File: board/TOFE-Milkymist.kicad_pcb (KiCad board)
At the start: 2 copper layers, 1 part

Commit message: Creating TOFE-Milkymist!
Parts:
- removed the U? at (148.4, 164.6)
- added U?: TOFE_Milkymist_Expansion_Board_8x_FullHeight, TOFE_8X_FullHeight, F.Cu at (125.1, 196.7)

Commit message: Initial version from on 2015-11-03
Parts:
- removed U?: TOFE_Milkymist_Expansion_Board_8x_FullHeight, TOFE_8X_FullHeight
- added 1PIN: P***, MH-4MM, F.Cu at (180.8, 64.5)
- added 1PIN: P***, MH-4MM, F.Cu at (181.1, 52.8)
- added C1: 1uF, SM0603, F.Cu at (106.6, 127.4)
- added C10: 100uF, SM1210, B.Cu at (126.4, 93.2)
- added C11: 0.1uF, SM0603, B.Cu at (121.5, 106.7)
- added C12: 1uF, SM0603, B.Cu at (119.9, 106.7)
- added C13: 0.1uF, SM0603, F.Cu at (121.6, 102.6)
- added C14: 3.3uF, SM0603, B.Cu at (121.6, 102.6)
- added C15: 22nF, SM0603, F.Cu at (116.8, 102.3)
- added C16: 1uF, SM0603, B.Cu at (113.5, 108.4)
- added C17: 100uF, SM1210, B.Cu at (126.4, 97.7)
- added C18: 220uF, C_Electrolytic, F.Cu at (107.2, 92.2)
- added C19: 20pF, SM0603, B.Cu at (123.9, 123.6)
- added C2: 1uF, SM0603, B.Cu at (106.1, 117.8)
- added C20: 1uF, SM0603, F.Cu at (108.1, 100.8)
- added C21: 220pF, SM0603, B.Cu at (106.1, 107.6)
- added C22: 220pF, SM0603, B.Cu at (106.1, 100.8)
- added C23: 20pF, SM0603, B.Cu at (112.2, 123.6)
- added C24: 220uF, C_Electrolytic, F.Cu at (117.9, 92.2)
- added C25: 1uF, SM0603, F.Cu at (108.1, 104.1)
- added C26: 220pF, SM0603, B.Cu at (106.1, 110.9)
- added C27: 220pF, SM0603, B.Cu at (106.1, 104.1)
- added C28: 0.1uF, SM0603, F.Cu at (128.7, 101.3)
- added C29: 0.1uF, SM0603_Capa, F.Cu at (140.5, 126.5)
- added C3: 1uF, SM0603, B.Cu at (106.1, 114.7)
- added C30: 0.1uF, SM0603_Capa, F.Cu at (113.7, 72.3)
- added C31: 0.1uF, SM0603_Capa, F.Cu at (109.6, 72.3)
- added C32: 0.1uF, SM0603_Capa, F.Cu at (107.6, 72.3)
- added C33: 0.1uF, SM0603, F.Cu at (111.6, 72.3)
- added C34: 0.1uF, SM0603_Capa_new, F.Cu at (160.3, 56.4)
- added C35: 0.1uF, SM0603_Capa_new, F.Cu at (172.0, 59.7)
- added C36: 15pF, SM0603_Capa, F.Cu at (176.3, 49.3)
- added C37: 15pF, SM0603_Capa, F.Cu at (172.2, 49.3)
- added C38: 0.1uF, SM0603_Capa_new, F.Cu at (115.1, 81.3)
- added C39: 10uF, SM0603_Capa_new, F.Cu at (95.2, 52.8)
- added C4: 220pF, SM0603, B.Cu at (106.6, 125.2)
- added C5: 0.1uF, SM0603, F.Cu at (126.9, 105.3)
- added C6: 2.2uF, SM0603, B.Cu at (105.1, 121.1)
- added C7: 0.1uF, SM0603, F.Cu at (125.4, 109.7)
- added C8: 0.1uF, SM0603, F.Cu at (112.5, 117.0)
- added C9: 1uF, SM0603, F.Cu at (112.5, 118.8)
- added CON1: AUDIO_JACK_3535NG, 3.5MM_Stereo_Jack_Socket, F.Cu at (88.3, 118.6)
- added CON2: AUDIO_JACK_3535NG, 3.5MM_Stereo_Jack_Socket, F.Cu at (88.3, 127.4)
- added CON3: AUDIO_JACK_3535NG, 3.5MM_Stereo_Jack_Socket, F.Cu at (88.3, 109.7)
- added CON4: AUDIO_JACK_3535NG, 3.5MM_Stereo_Jack_Socket, F.Cu at (88.3, 100.8)
- added D1: IR-LED, LEDV, F.Cu at (92.5, 59.7)
- added D2: LED, LED-0805-New, F.Cu at (171.7, 77.2)
- added D3: DIODE, DO214AA, F.Cu at (154.2, 53.6)
- added D4: DIODE, DO214AA, F.Cu at (134.1, 128.5)
- added D5: LED, LED-0805-New, F.Cu at (171.7, 87.4)
- added D6: LED, LED-0805-New, F.Cu at (171.7, 83.8)
- added D7: LED, LED-0805-New, F.Cu at (171.7, 80.5)
- added G***: LOGO, LOGO, F.Cu at (156.5, 122.2)
- added GS1: GS2, PIN_ARRAY_2X1, F.Cu at (168.7, 54.4)
- added GS2: GS2, PIN_ARRAY_2X1, F.Cu at (168.7, 60.5)
- added IC1: PC817, SMD_PC817, F.Cu at (153.9, 62.2)
- added J1: DB9, DB9_Female, F.Cu at (97.3, 79.8)
- added K1: CONN_2, ScrewTerm2_138MIL, F.Cu at (158.4, 40.1)
- added K2: CONN_2, ScrewTerm2_138MIL, F.Cu at (165.5, 40.1)
- added K3: CONN_3, ScrewTerm3_138MIL, F.Cu at (151.3, 40.1)
- added K4: CONN_3, ScrewTerm3_138MIL, F.Cu at (177.5, 40.1)
- added K5: CONN_2, ScrewTerm2_138MIL, F.Cu at (184.7, 40.1)
- added K6: CONN_2, ScrewTerm2_138MIL, F.Cu at (191.8, 40.1)
- added K7: CONN_2, ScrewTerm2_138MIL, F.Cu at (132.1, 40.1)
- added K8: CONN_2, ScrewTerm2_138MIL, F.Cu at (139.2, 40.1)
- added L1: 4.7uH, SM0805, F.Cu at (125.4, 101.5)
- added L2: 4.7uH, SM0805, F.Cu at (112.5, 115.0)
- added L3: 4.7uH, SM0805, F.Cu at (160.3, 60.5)
- added P2: CONN_4X2, pin_array_4x2, F.Cu at (125.0, 68.6)
- added P4: CONN_6X2, pin_array_6x2, F.Cu at (187.2, 96.5)
- added P5: CONN_6X2, pin_array_6x2, F.Cu at (187.2, 117.2)
- added Q1: TRANSISTOR-NPN, SOT23-TRANSISTOR-NPN, F.Cu at (98.6, 61.5)
- added R1: 1K, SM0603, F.Cu at (106.6, 129.7)
- added R10: 27.4, SM0603, F.Cu at (124.1, 116.8)
- added R11: 4.75K, SM0603, F.Cu at (125.4, 112.7)
- added R12: 4.75K, SM0603, F.Cu at (129.3, 123.2)
- added R13: 4.75K, SM0603, F.Cu at (127.4, 115.0)
- added R14: 0R, SM0603, B.Cu at (117.9, 104.1)
- added R15: 10K, SM0603, F.Cu at (140.5, 134.1)
- added R16: R, SM0603, F.Cu at (121.6, 100.5)
- added R17: 1M, SM0402, F.Cu at (118.0, 118.6)
- added R18: 10K, SM0603, F.Cu at (106.1, 107.6)
- added R19: 10K, SM0603, F.Cu at (106.1, 100.8)
- added R2: 6.81K, SM0603, F.Cu at (106.1, 117.8)
- added R20: 10K, SM0603, F.Cu at (106.1, 110.9)
- added R21: 10K, SM0603, F.Cu at (106.1, 104.1)
- added R22: 10K, SM0603, F.Cu at (138.2, 134.1)
- added R23: 47R, SM0603_Resistor_new, F.Cu at (98.6, 57.4)
- added R24: 1K, SM0603_Resistor_new, F.Cu at (95.2, 49.0)
- added R25: 220R, SM0603_Resistor_new, F.Cu at (160.6, 49.3)
- added R26: 220R, SM0603_Resistor_new, F.Cu at (151.4, 49.3)
- added R27: 220R, SM0603_Resistor_new, F.Cu at (162.8, 49.3)
- added R28: 220R, SM0603_Resistor_new, F.Cu at (154.4, 69.3)
- added R29: 60R, SM0603_Resistor_new, F.Cu at (174.2, 49.3)
- added R3: 6.81K, SM0603, F.Cu at (106.1, 114.7)
- added R30: 2K2, SM0603_Capa_new, F.Cu at (102.1, 63.2)
- added R31: 680R, RES_NET4, F.Cu at (189.5, 68.6)
- added R32: 10K, RES_NET4, F.Cu at (176.9, 82.0)
- added R33: 10K, SM0603_Resistor_new, F.Cu at (102.1, 60.2)
- added R4: 47K, SM0603, B.Cu at (106.6, 129.7)
- added R5: 6.81K, SM0603, F.Cu at (108.1, 114.7)
- added R6: 6.81K, SM0603, F.Cu at (108.1, 117.8)
- added R7: 47R, SM0603, F.Cu at (106.6, 125.2)
- added R8: 2.2K, SM0603, B.Cu at (105.1, 123.1)
- added R9: 27.4, SM0603, F.Cu at (124.1, 118.8)
- added SW1: SW_PUSH, Switch_SMD_new, F.Cu at (189.5, 78.0)
- added SW2: SW_PUSH, Switch_SMD_new, F.Cu at (194.8, 68.6)
- added SW3: SW_PUSH, Switch_SMD_new, F.Cu at (189.5, 59.2)
- added SW4: SW_PUSH, Switch_SMD_new, F.Cu at (184.2, 68.8)
- added U1: LM4550, LQFP48, F.Cu at (118.3, 109.7)
- added U2: 7805_N, DPAK2, F.Cu at (125.9, 95.4)
- added U3: ST3232CDR, ssop-16, F.Cu at (110.6, 78.9)
- added U4: SN74LVC1G17, SOT23-5_SN74LVC1G17DBVR, F.Cu at (163.6, 57.4)
- added U5: ISL83490, SOIC-8_ISL83490, F.Cu at (175.8, 56.6)
- added U6: IR-RX, IR_REC_TH, F.Cu at (92.5, 51.1)
- added U7: 24AA01/24LC01B, SOT23-5_24AA01, F.Cu at (139.4, 130.3)
- added U8: TIMVIDEOS-PCIE-8X, NumatoOpsis_PCIe_8X_HL_NW_110x110, F.Cu at (88.1, 143.8)
- added X1: CRYSTAL, HC-49V, F.Cu at (118.0, 123.6)
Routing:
- net /GND: track 0.00 -> 568.0 mm, vias 0 -> 113
- net /VCC3V3: track 0.00 -> 492.0 mm, vias 0 -> 11
- net /IR_OUT: track 0.00 -> 151.0 mm
- net /VCC12V: track 0.00 -> 141.5 mm, vias 0 -> 3
- net /IR_EN: track 0.00 -> 131.8 mm
- net /AGND: track 0.00 -> 130.0 mm, vias 0 -> 29
- net /VCC5V0: track 0.00 -> 104.4 mm, vias 0 -> 2
- net /RS232-RX1: track 0.00 -> 99.6 mm
- net /RS232-TX1: track 0.00 -> 98.2 mm
- net /RS232-TX2: track 0.00 -> 98.1 mm
- net /RS232-RX2: track 0.00 -> 97.3 mm
- net /SW2: track 0.00 -> 97.0 mm, vias 0 -> 1
- net /SW1: track 0.00 -> 94.8 mm, vias 0 -> 3
- net /DMX_TX: track 0.00 -> 89.1 mm
- net /DMX_RX: track 0.00 -> 88.9 mm
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- added copper zone on B.Cu, net /AGND
- added copper zone on F.Cu, net /AGND
- added copper zone on B.Cu, net /GND
- added copper zone on F.Cu, net /GND
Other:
- board outline added: 110 x 111.3 mm
- net class Default: clearance 0.254 -> 0.1524; trace_width 0.254 -> 0.2032; via_dia 0.889 -> 0.6096; via_drill 0.635 -> 0.3048
- rule trace_clearance: 0.254 -> 0.1524
- rule trace_min: 0.254 -> 0.2032
- rule via_min_drill: 0.508 -> 0.3048
- rule via_min_size: 0.889 -> 0.6096
- board text added: "1"
- board text added: "11"
- board text added: "12"
- board text added: "2"
- board text added: "3V3"
- board text added: "DMXIN"
- board text added: "DMXOUT"
- board text added: "EXPANSION CONNECTORS"
- board text added: "GND"
- board text added: "GPIO'S"
- board text added: "HP OUT"
- board text added: "IN"
- board text added: "IO1"
- board text added: "IO2"
- board text added: "IO3"
- board text added: "IO4"
- board text added: "IO5"
- board text added: "IO6"
- board text added: "LED1"
- board text added: "LED2"
- board text added: "LED3"
- board text added: "LED4"
- board text added: "LINE IN"
- board text added: "LINE OUT"
- board text added: "MIC"
- board text added: "MIDIIN"
- board text added: "MIDIOUT"
- board text added: "OUT"
- board text added: "RS232"
- board text added: "TOFE Milkymist Compatibility Expansion Board www.numato.com"

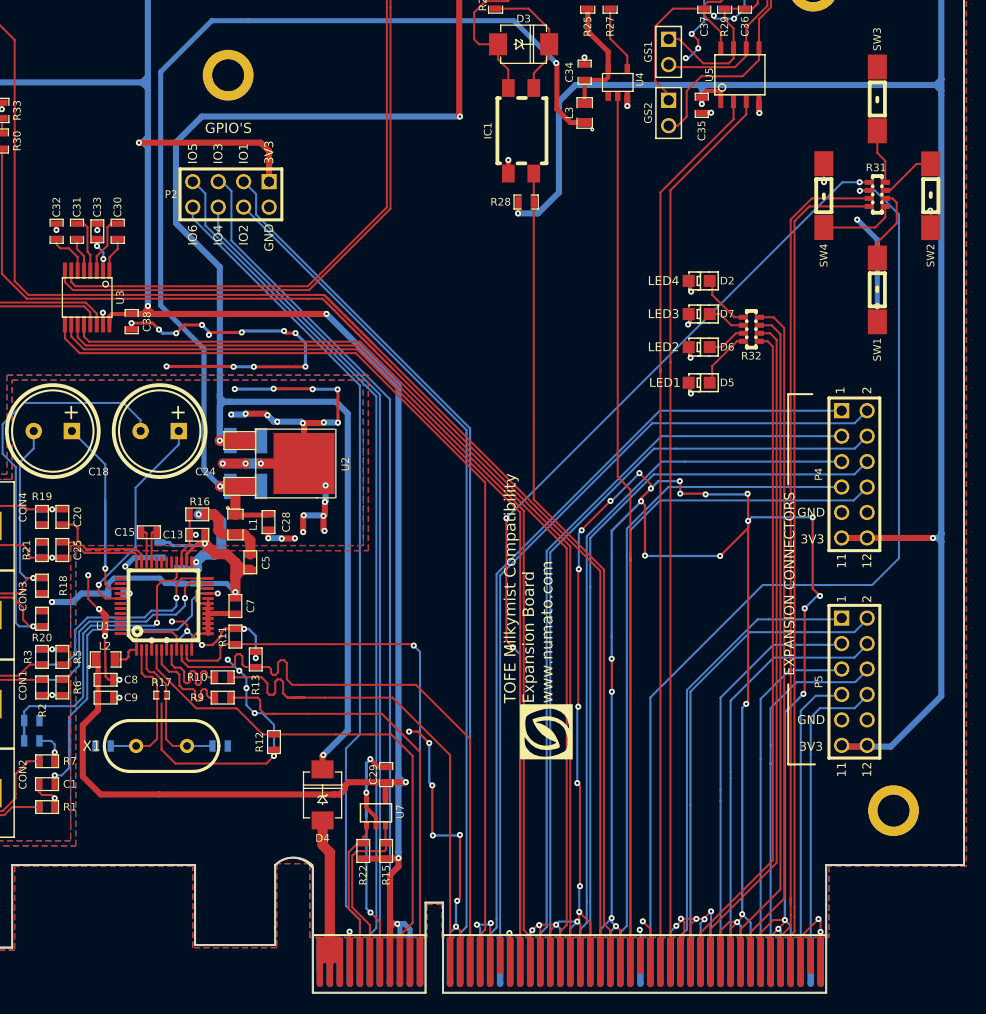
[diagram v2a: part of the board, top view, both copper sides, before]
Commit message: Changing mounting holes arrangement.
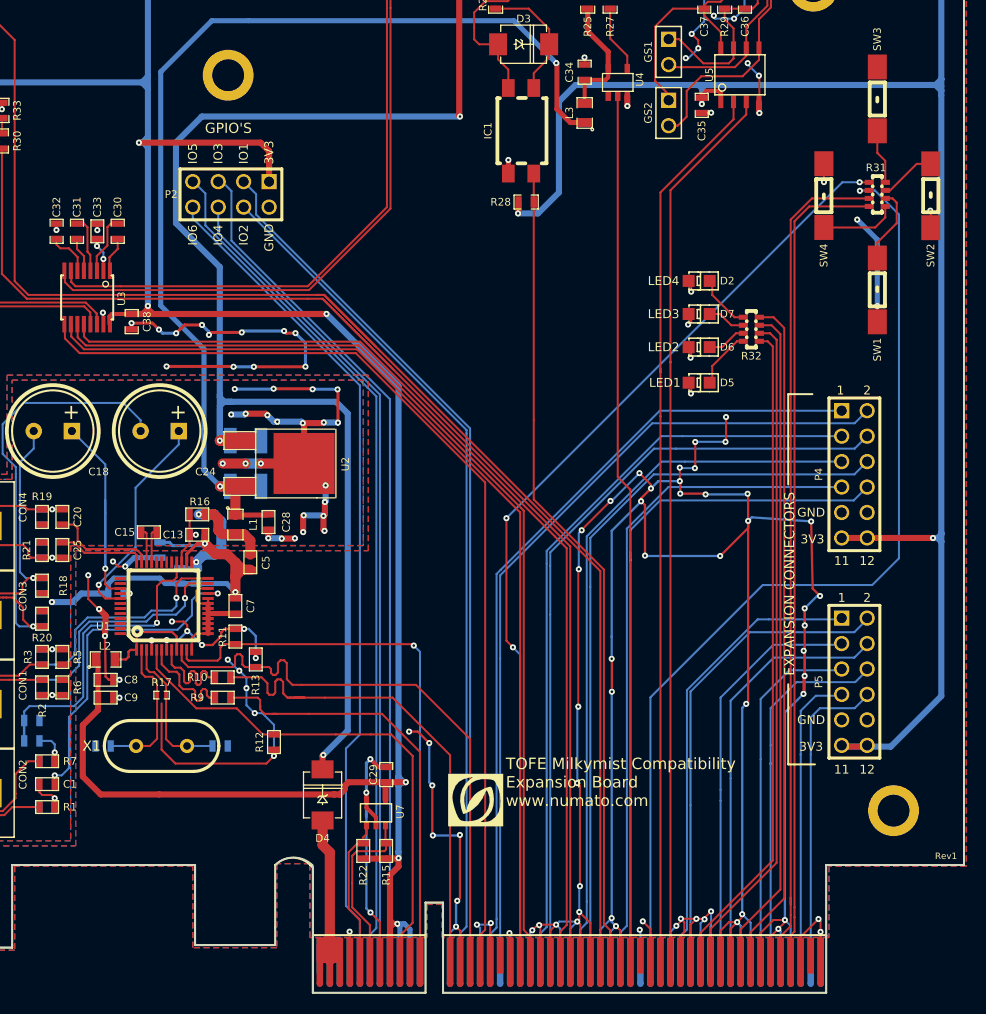
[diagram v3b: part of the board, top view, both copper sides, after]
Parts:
- removed 1PIN (x2): P***, MH-4MM
- U3: footprint ssop-16 -> TSSOP-16
- moved G*** 9.88 mm to (149.4, 129.0), turned to 0 degrees
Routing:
- net /GND: track 568.0 -> 596.1 mm, vias 113 -> 124
- net /12V: track 31.8 -> 36.4 mm
- net /GPIO2: track 84.7 -> 87.0 mm
- net /AC97_SDI: track 51.3 -> 53.6 mm
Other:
- board text added: "Rev1"

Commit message: More changes to mechanical holes.
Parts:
- U8: footprint NumatoOpsis_PCIe_8X_HL_NW_110x110 -> NumatoOpsis_PCIe_8X_HL_NW_1
- moved U8 57.3 mm to (145.3, 148.3)
- moved K1 5.13 mm to (158.4, 35.0)
- moved K2 5.13 mm to (165.5, 35.0)
- moved K3 5.13 mm to (151.3, 35.0)
- moved K4 5.13 mm to (177.5, 35.0)
- moved K5 5.13 mm to (184.7, 35.0)
- moved K6 5.13 mm to (191.8, 35.0)
- moved K7 5.13 mm to (132.1, 35.0)
- moved K8 5.13 mm to (139.2, 35.0)
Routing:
- net /GND: track 596.1 -> 690.0 mm, vias 124 -> 125
- net /VCC3V3: track 492.0 -> 510.0 mm
- net /12V: track 36.4 -> 47.9 mm
- net /MIDI_IN_PIN5: track 23.9 -> 30.0 mm
- net /VCC5V0: track 104.4 -> 98.4 mm
- net /RS232-IN2: track 76.3 -> 81.8 mm
- net /DMX-DATA_OUT-: track 31.6 -> 37.1 mm
- net /DMX-DATA_OUT+: track 40.1 -> 45.5 mm
- net /DMX-DATA_IN-: track 25.9 -> 31.2 mm
- net /VCC12V: track 141.5 -> 146.7 mm
- net /MIDI_OUT_PIN4: track 8.92 -> 14.1 mm
- net /MIDI_OUT_PIN5: track 9.49 -> 14.6 mm
- net /MIDI_IN_PIN4: track 8.43 -> 13.6 mm
- net /RS232-OUT2: track 66.4 -> 71.5 mm
- net /DMX-DATA_IN+: track 39.2 -> 44.3 mm
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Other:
- board size 110 x 111.3 mm -> 110 x 116.3 mm

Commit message: Fixing part reference.
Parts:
- U8: value TIMVIDEOS-PCIE-8X -> TOFE-8X
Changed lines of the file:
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@@
       (effects (font (size 1.016 1.016) (thickness 0.254)))
     )
-    (fp_text value TIMVIDEOS-PCIE-8X (at 19.175 -10.75) (layer F.SilkS) hide
+    (fp_text value TOFE-8X (at 19.175 -10.75) (layer F.SilkS) hide
       (effects (font (size 1.016 1.016) (thickness 0.254)))
     )

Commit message: Updated version sent to production.
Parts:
- U3: footprint TSSOP-16 -> SO16_N
- U8: footprint NumatoOpsis_PCIe_8X_HL_NW_1 -> NumatoOpsis_PCIe_8X_HL_NW_123
- moved U3 1.91 mm to (108.7, 79.0)
- moved C30 1.27 mm to (112.4, 72.3)
- moved C31 1.27 mm to (108.3, 72.3)
- moved C32 1.27 mm to (106.3, 72.3)
- moved C33 1.27 mm to (110.4, 72.3)
- moved C38 0.25 mm to (115.3, 81.3)
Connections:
- J1 pad 2: /RS232-OUT1 -> /RS232-IN1
- J1 pad 3: /RS232-IN1 -> /RS232-OUT1
- R24 pad 2: N-0000070 -> N-0000075
- U6 pad 1: /VCC3V3 -> N-0000075
- U6 pad 3: N-0000070 -> /VCC3V3
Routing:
- net /GND: track 690.0 -> 730.7 mm, vias 125 -> 135
- net /12V: track 47.9 -> 57.8 mm, vias 0 -> 1
- net /RS232-OUT1: track 20.6 -> 13.9 mm
- net /VCC3V3: track 510.0 -> 515.5 mm, vias 11 -> 12
- net /RS232-IN2: track 81.8 -> 86.3 mm
- net /RS232-OUT2: track 71.5 -> 75.7 mm
- net /RS232-RX2: track 99.6 -> 103.6 mm
- net /VCC5V0: track 98.4 -> 102.5 mm
- net /RS232-TX2: track 100.4 -> 104.3 mm
- net /RS232-TX1: track 100.5 -> 103.5 mm
- net N-0000075: track 0.00 -> 2.85 mm
- net N-0000070: track 2.85 -> 0.00 mm
- net /RS232-RX1: track 101.9 -> 104.5 mm
- net N-00000104: track 3.47 -> 5.02 mm
- net N-00000110: track 4.54 -> 3.13 mm
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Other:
- board text added: "Rev2"
- board text removed: "Rev1"
